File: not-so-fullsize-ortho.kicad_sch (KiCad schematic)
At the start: 153 parts, among them K0 Home, K1 Tab, K10 O, K11 P, K12 Back Space, K13 Delete, K14 1, K15 2, K16 3, K17 End, K18 Esc, K19 A, K2 Q, K20 S, K21 D, K22 F, K23 G, K24 H, K25 J, K26 K, K27 L, K28 ;, K29 ', K3 W, K30 Return, K31 4, K32 5, K33 6, K34 Vol +, K35 Shift, K36 Z, K37 X, K38 C, K39 V, K4 E, K40 B, K41 N, K42 M, K43 ,, K44 ., K45 /, K46 Shift, K47 7, K48 8, K49 9, K5 R, K50 &uarr;, K51 Vol -, K52 Ctrl, K53 Alt, K54 Super, K55 &dArr;, K56 Blank, K57 &uArr;, K58 Alt, K59 Fn, K6 T, K60 0, K61 Enter, K62 &larr;, K63 &darr;, K64 &rarr;, K7 Y, K8 U, K9 I, U1 Pico

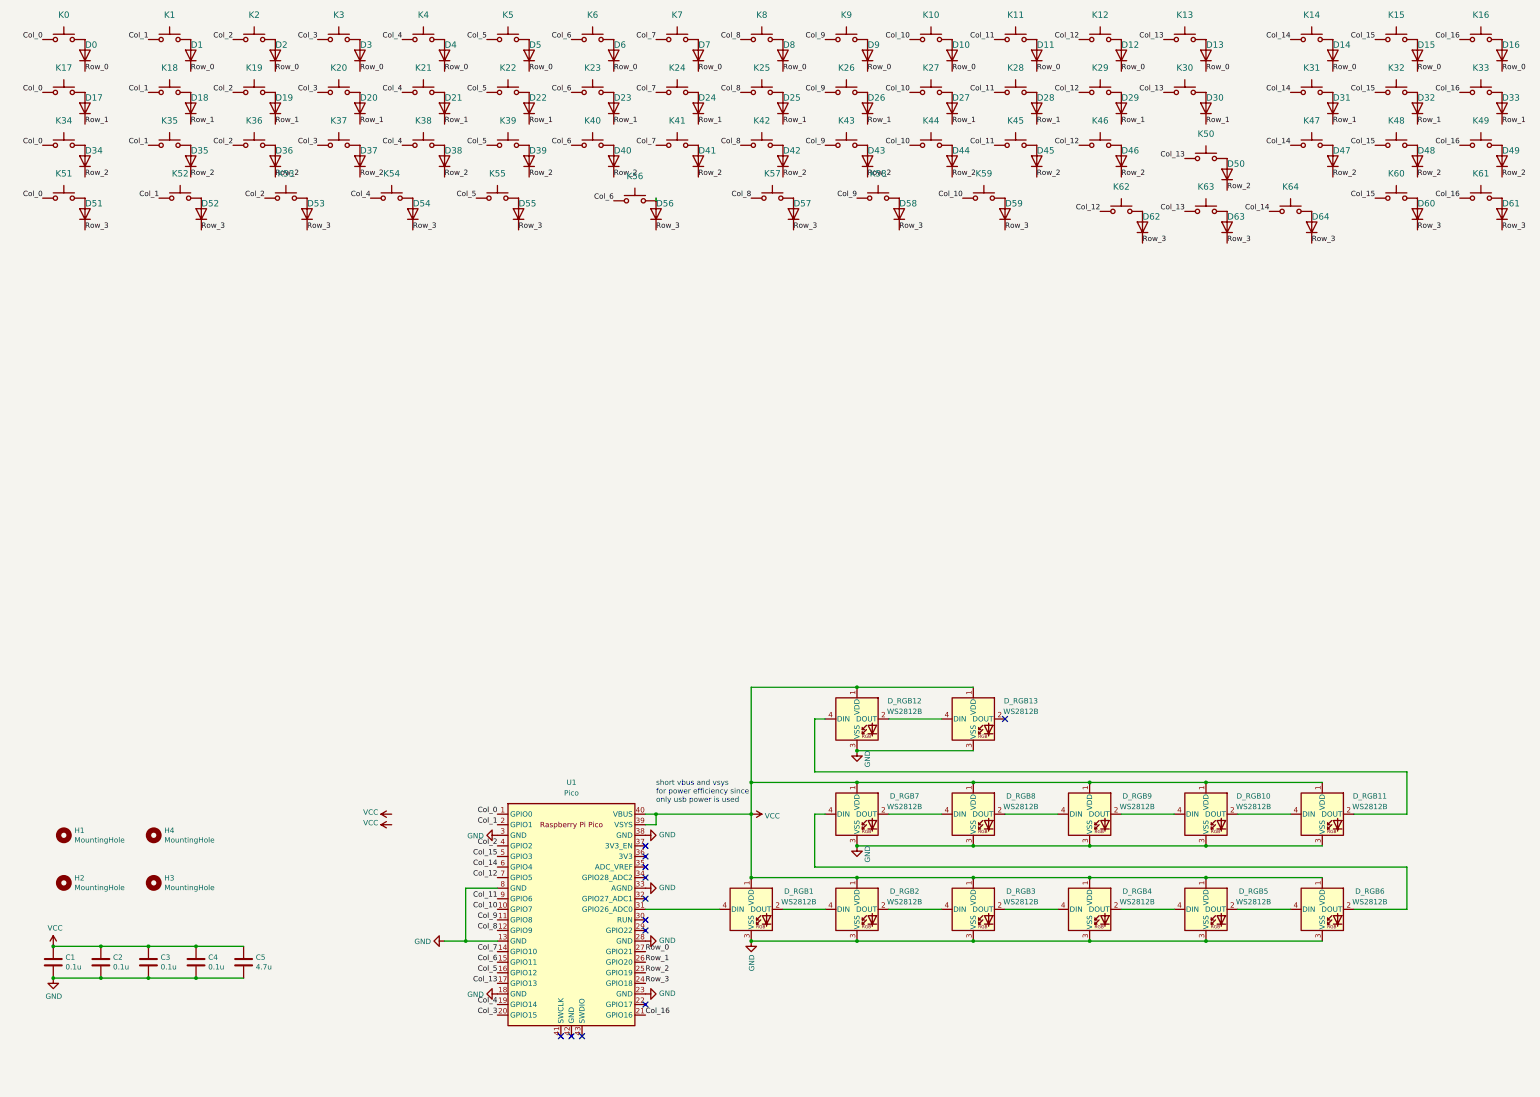
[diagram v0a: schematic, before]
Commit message: rework for rp2040 (not pico dev board)
kicad 8 version bump, much better schematic, some DRC rules, start with layout of rp2040/USB portion of board, will need to reroute all the rows/cols when done.
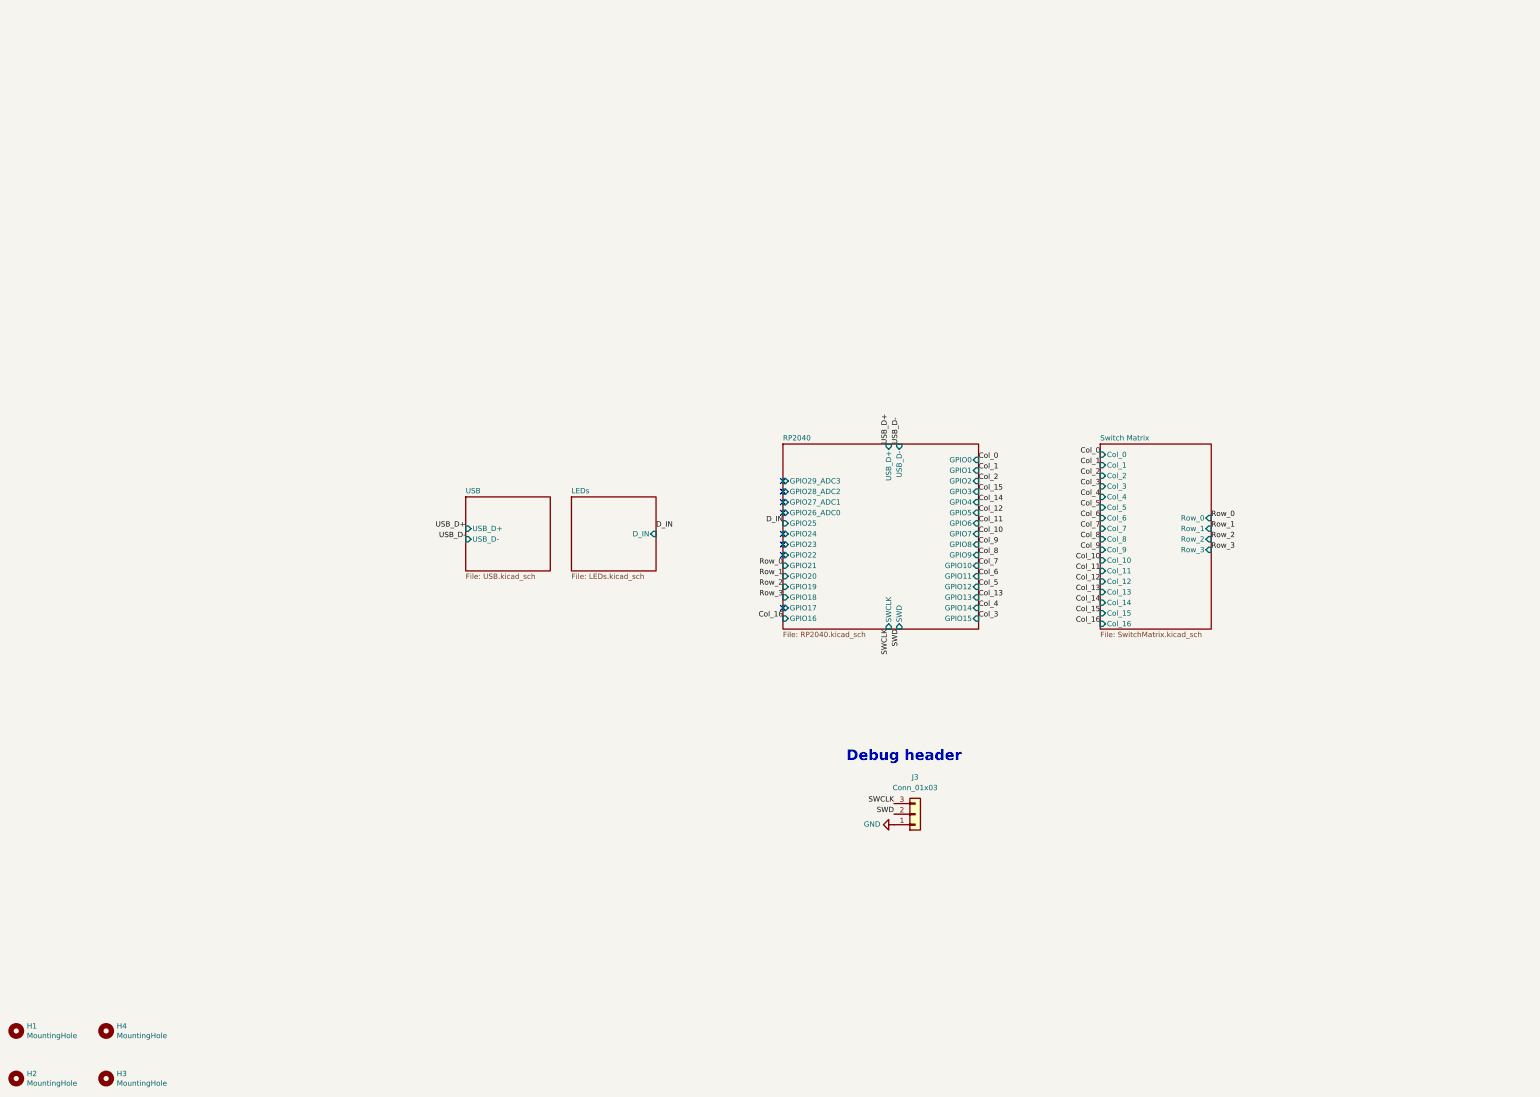
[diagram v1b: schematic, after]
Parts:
- removed C1, C2, C3, C4: 0.1u, Capacitor_SMD:C_0805_2012Metric_Pad1.18x1.45mm_HandSolder, symbol Device:C
- removed C5: 4.7u, Capacitor_SMD:C_0805_2012Metric_Pad1.18x1.45mm_HandSolder, symbol Device:C
- removed D0, D1, D10, D11, D12, D13, D14, D15, D16, D17, D18, D19, D2, D20, D21, D22, D23, D24, D25, D26, D27, D28, D29, D3, D30, D31, D32, D33, D34, D35, D36, D37, D38, D39, D4, D40, D41, D42, D43, D44, D45, D46, D47, D48, D49, D5, D50, D51, D52, D53, D54, D55, D56, D57, D58, D59, D6, D60, D61, D62, D63, D64, D7, D8, D9: D, Diode_SMD:D_0805_2012Metric_Pad1.15x1.40mm_HandSolder, symbol Device:D
- removed D_RGB1: WS2812B, Connector_JST:JST_XH_B5B-XH-A_1x05_P2.50mm_Vertical, symbol LED:WS2812B
- removed D_RGB10, D_RGB11, D_RGB12, D_RGB13, D_RGB2, D_RGB3, D_RGB4, D_RGB5, D_RGB6, D_RGB7, D_RGB8, D_RGB9: WS2812B, LED_SMD:LED_WS2812B_PLCC4_5.0x5.0mm_P3.2mm, symbol LED:WS2812B
- removed K0: Home, Switch_Keyboard_Cherry_MX:SW_Cherry_MX_PCB_1.00u, symbol Switch:SW_Push
- removed K1: Tab, Switch_Keyboard_Cherry_MX:SW_Cherry_MX_PCB_1.00u, symbol Switch:SW_Push
- removed K10: O, Switch_Keyboard_Cherry_MX:SW_Cherry_MX_PCB_1.00u, symbol Switch:SW_Push
- removed K11: P, Switch_Keyboard_Cherry_MX:SW_Cherry_MX_PCB_1.00u, symbol Switch:SW_Push
- removed K12: Back Space, Switch_Keyboard_Cherry_MX:SW_Cherry_MX_PCB_1.00u, symbol Switch:SW_Push
- removed K13: Delete, Switch_Keyboard_Cherry_MX:SW_Cherry_MX_PCB_1.00u, symbol Switch:SW_Push
- removed K14: 1, Switch_Keyboard_Cherry_MX:SW_Cherry_MX_PCB_1.00u, symbol Switch:SW_Push
- removed K15: 2, Switch_Keyboard_Cherry_MX:SW_Cherry_MX_PCB_1.00u, symbol Switch:SW_Push
- removed K16: 3, Switch_Keyboard_Cherry_MX:SW_Cherry_MX_PCB_1.00u, symbol Switch:SW_Push
- removed K17: End, Switch_Keyboard_Cherry_MX:SW_Cherry_MX_PCB_1.00u, symbol Switch:SW_Push
- removed K18: Esc, Switch_Keyboard_Cherry_MX:SW_Cherry_MX_PCB_1.00u, symbol Switch:SW_Push
- removed K19: A, Switch_Keyboard_Cherry_MX:SW_Cherry_MX_PCB_1.00u, symbol Switch:SW_Push
- removed K2: Q, Switch_Keyboard_Cherry_MX:SW_Cherry_MX_PCB_1.00u, symbol Switch:SW_Push
- removed K20: S, Switch_Keyboard_Cherry_MX:SW_Cherry_MX_PCB_1.00u, symbol Switch:SW_Push
- removed K21: D, Switch_Keyboard_Cherry_MX:SW_Cherry_MX_PCB_1.00u, symbol Switch:SW_Push
- removed K22: F, Switch_Keyboard_Cherry_MX:SW_Cherry_MX_PCB_1.00u, symbol Switch:SW_Push
- removed K23: G, Switch_Keyboard_Cherry_MX:SW_Cherry_MX_PCB_1.00u, symbol Switch:SW_Push
- removed K24: H, Switch_Keyboard_Cherry_MX:SW_Cherry_MX_PCB_1.00u, symbol Switch:SW_Push
- removed K25: J, Switch_Keyboard_Cherry_MX:SW_Cherry_MX_PCB_1.00u, symbol Switch:SW_Push
- removed K26: K, Switch_Keyboard_Cherry_MX:SW_Cherry_MX_PCB_1.00u, symbol Switch:SW_Push
- removed K27: L, Switch_Keyboard_Cherry_MX:SW_Cherry_MX_PCB_1.00u, symbol Switch:SW_Push
- removed K28: ;, Switch_Keyboard_Cherry_MX:SW_Cherry_MX_PCB_1.00u, symbol Switch:SW_Push
- removed K29: ', Switch_Keyboard_Cherry_MX:SW_Cherry_MX_PCB_1.00u, symbol Switch:SW_Push
- removed K3: W, Switch_Keyboard_Cherry_MX:SW_Cherry_MX_PCB_1.00u, symbol Switch:SW_Push
- removed K30: Return, Switch_Keyboard_Cherry_MX:SW_Cherry_MX_PCB_1.00u, symbol Switch:SW_Push
- removed K31: 4, Switch_Keyboard_Cherry_MX:SW_Cherry_MX_PCB_1.00u, symbol Switch:SW_Push
- removed K32: 5, Switch_Keyboard_Cherry_MX:SW_Cherry_MX_PCB_1.00u, symbol Switch:SW_Push
- removed K33: 6, Switch_Keyboard_Cherry_MX:SW_Cherry_MX_PCB_1.00u, symbol Switch:SW_Push
- removed K34: Vol +, Switch_Keyboard_Cherry_MX:SW_Cherry_MX_PCB_1.00u, symbol Switch:SW_Push
- removed K35, K46: Shift, Switch_Keyboard_Cherry_MX:SW_Cherry_MX_PCB_1.00u, symbol Switch:SW_Push
- removed K36: Z, Switch_Keyboard_Cherry_MX:SW_Cherry_MX_PCB_1.00u, symbol Switch:SW_Push
- removed K37: X, Switch_Keyboard_Cherry_MX:SW_Cherry_MX_PCB_1.00u, symbol Switch:SW_Push
- removed K38: C, Switch_Keyboard_Cherry_MX:SW_Cherry_MX_PCB_1.00u, symbol Switch:SW_Push
- removed K39: V, Switch_Keyboard_Cherry_MX:SW_Cherry_MX_PCB_1.00u, symbol Switch:SW_Push
- removed K4: E, Switch_Keyboard_Cherry_MX:SW_Cherry_MX_PCB_1.00u, symbol Switch:SW_Push
- removed K40: B, Switch_Keyboard_Cherry_MX:SW_Cherry_MX_PCB_1.00u, symbol Switch:SW_Push
- removed K41: N, Switch_Keyboard_Cherry_MX:SW_Cherry_MX_PCB_1.00u, symbol Switch:SW_Push
- removed K42: M, Switch_Keyboard_Cherry_MX:SW_Cherry_MX_PCB_1.00u, symbol Switch:SW_Push
- removed K43: ,, Switch_Keyboard_Cherry_MX:SW_Cherry_MX_PCB_1.00u, symbol Switch:SW_Push
- removed K44: ., Switch_Keyboard_Cherry_MX:SW_Cherry_MX_PCB_1.00u, symbol Switch:SW_Push
- removed K45: /, Switch_Keyboard_Cherry_MX:SW_Cherry_MX_PCB_1.00u, symbol Switch:SW_Push
- removed K47: 7, Switch_Keyboard_Cherry_MX:SW_Cherry_MX_PCB_1.00u, symbol Switch:SW_Push
- removed K48: 8, Switch_Keyboard_Cherry_MX:SW_Cherry_MX_PCB_1.00u, symbol Switch:SW_Push
- removed K49: 9, Switch_Keyboard_Cherry_MX:SW_Cherry_MX_PCB_1.00u, symbol Switch:SW_Push
- removed K5: R, Switch_Keyboard_Cherry_MX:SW_Cherry_MX_PCB_1.00u, symbol Switch:SW_Push
- removed K50: &uarr;, Switch_Keyboard_Cherry_MX:SW_Cherry_MX_PCB_1.00u, symbol Switch:SW_Push
- removed K51: Vol -, Switch_Keyboard_Cherry_MX:SW_Cherry_MX_PCB_1.00u, symbol Switch:SW_Push
- removed K52: Ctrl, Switch_Keyboard_Cherry_MX:SW_Cherry_MX_PCB_1.25u, symbol Switch:SW_Push
- removed K53, K58: Alt, Switch_Keyboard_Cherry_MX:SW_Cherry_MX_PCB_1.25u, symbol Switch:SW_Push
- removed K54: Super, Switch_Keyboard_Cherry_MX:SW_Cherry_MX_PCB_1.25u, symbol Switch:SW_Push
- removed K55: &dArr;, Switch_Keyboard_Cherry_MX:SW_Cherry_MX_PCB_1.25u, symbol Switch:SW_Push
- removed K56: Blank, Switch_Keyboard_Cherry_MX:SW_Cherry_MX_PCB_2.00u, symbol Switch:SW_Push
- removed K57: &uArr;, Switch_Keyboard_Cherry_MX:SW_Cherry_MX_PCB_1.25u, symbol Switch:SW_Push
- removed K59: Fn, Switch_Keyboard_Cherry_MX:SW_Cherry_MX_PCB_1.25u, symbol Switch:SW_Push
- removed K6: T, Switch_Keyboard_Cherry_MX:SW_Cherry_MX_PCB_1.00u, symbol Switch:SW_Push
- removed K60: 0, Switch_Keyboard_Cherry_MX:SW_Cherry_MX_PCB_1.00u, symbol Switch:SW_Push
- removed K61: Enter, Switch_Keyboard_Cherry_MX:SW_Cherry_MX_PCB_1.00u, symbol Switch:SW_Push
- removed K62: &larr;, Switch_Keyboard_Cherry_MX:SW_Cherry_MX_PCB_1.00u, symbol Switch:SW_Push
- removed K63: &darr;, Switch_Keyboard_Cherry_MX:SW_Cherry_MX_PCB_1.00u, symbol Switch:SW_Push
- removed K64: &rarr;, Switch_Keyboard_Cherry_MX:SW_Cherry_MX_PCB_1.00u, symbol Switch:SW_Push
- removed K7: Y, Switch_Keyboard_Cherry_MX:SW_Cherry_MX_PCB_1.00u, symbol Switch:SW_Push
- removed K8: U, Switch_Keyboard_Cherry_MX:SW_Cherry_MX_PCB_1.00u, symbol Switch:SW_Push
- removed K9: I, Switch_Keyboard_Cherry_MX:SW_Cherry_MX_PCB_1.00u, symbol Switch:SW_Push
- removed U1: Pico, MCU_RaspberryPi_and_Boards:RPi_Pico_SMD_TH, symbol MCU_RaspberryPi_and_Boards:Pico
- added J3: Conn_01x03, Connector_PinHeader_2.54mm:PinHeader_1x03_P2.54mm_Vertical, symbol Connector_Generic:Conn_01x03
- H1, H2, H3, H4: footprint MountingHole:MountingHole_3.2mm_M3_DIN965 -> MountingHole:MountingHole_2.2mm_M2
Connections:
- net GND: now also J3.1 (Pin_1)
- new net SWCLK: J3.3 (Pin_3)
- new net SWD: J3.2 (Pin_2)
- no-connect marks 12 -> 8
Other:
- added sheet LEDs (LEDs.kicad_sch)
- added sheet RP2040 (RP2040.kicad_sch)
- added sheet Switch Matrix (SwitchMatrix.kicad_sch)
- added sheet USB (USB.kicad_sch)
- note added: "Debug header"
- note removed: "short vbus and vsys for power efficiency since only usb power is used"
- title: compact  -> "not-so-fullsize" ortho
- moved on the sheet: H1, H2, H3, H4

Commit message: layout rp2040 mwe
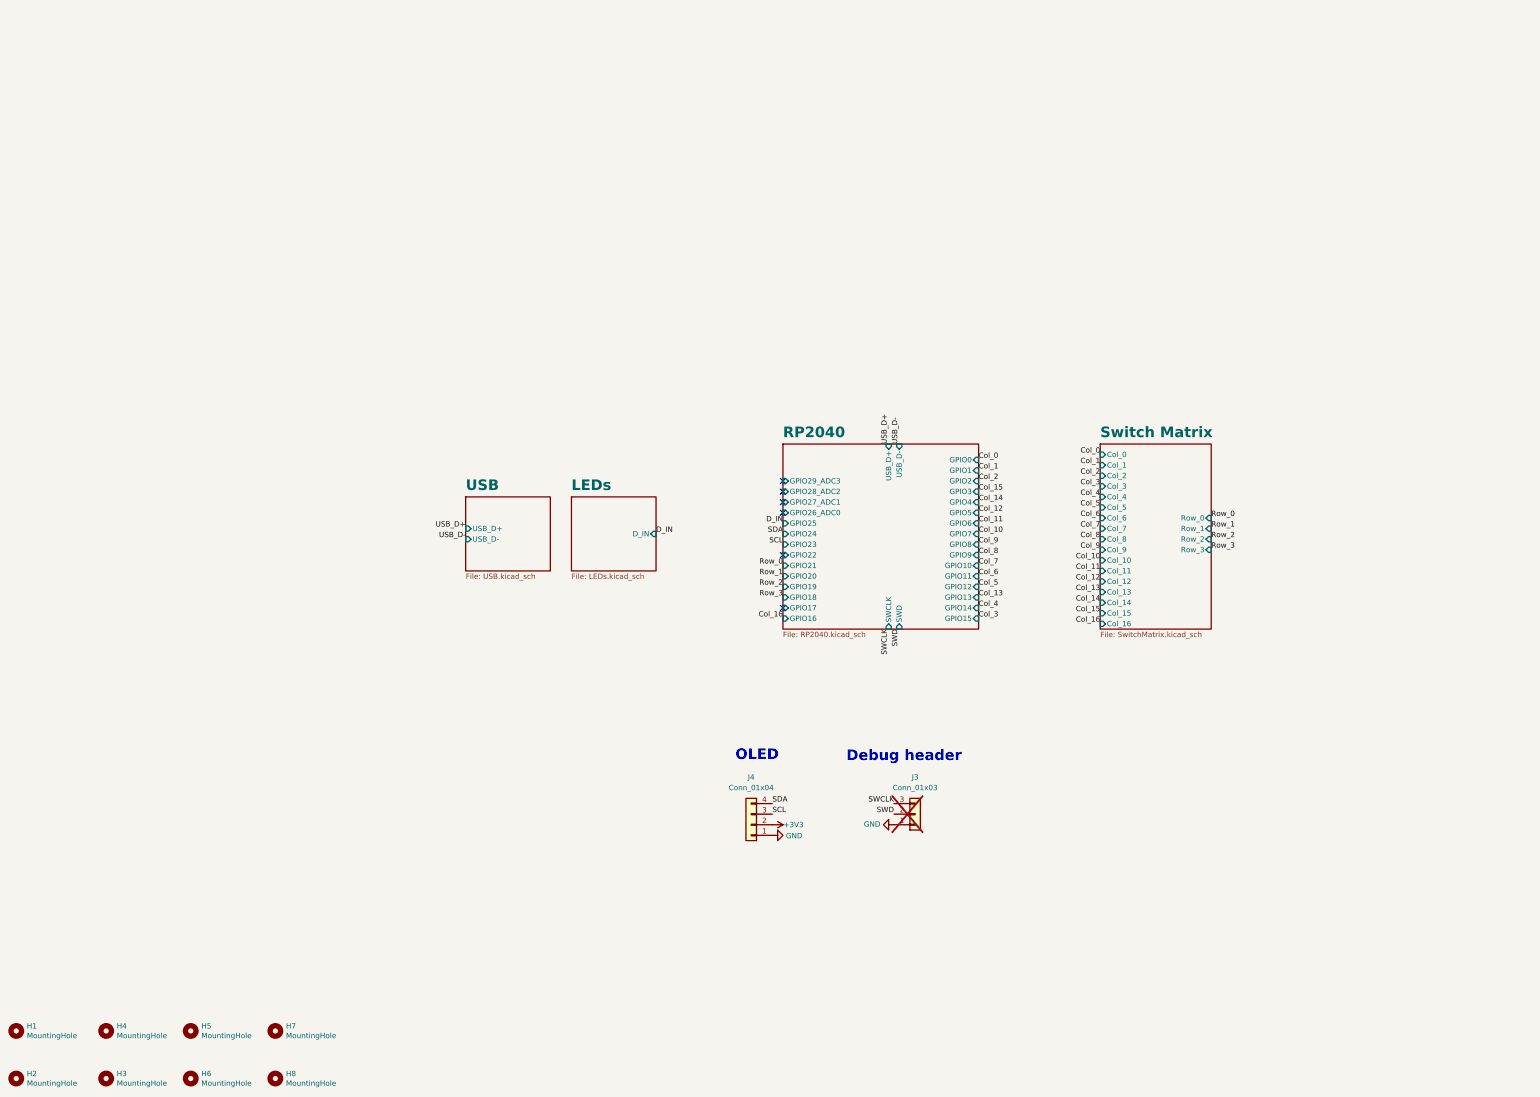
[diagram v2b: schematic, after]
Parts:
- added H5, H6, H7, H8: MountingHole, MountingHole:MountingHole_2.2mm_M2, symbol Mechanical:MountingHole
- added J4: Conn_01x04, Connector_PinSocket_2.54mm:PinSocket_1x04_P2.54mm_Vertical, symbol Connector_Generic:Conn_01x04
- J3: now not fitted
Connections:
- net GND: now also J4.1 (Pin_1)
- new net +3V3: J4.2 (Pin_2)
- new net SCL: J4.3 (Pin_3)
- new net SDA: J4.4 (Pin_4)
- no-connect marks 8 -> 6
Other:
- note added: "OLED"
